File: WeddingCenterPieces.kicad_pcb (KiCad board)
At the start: 2 copper layers, 80 x 57 mm, 58 parts, among them J1 USB_C_Receptacle_USB2.0_16P, J2 DBG, J5 WS2812, K1 SW_Push, K2 SW_Push, K3 SW_Push, K4 SW_Push, SW1 Btn_OnBoard, SW2 RST, SW3 BOOT, U1 RP2040, U2 TPD2E2U06, U4 TXS0101DBV, U5 W25Q128JVSIQ, U6 TVS0500DRV, U7 AP2112K-3.3, Y1 12MHz

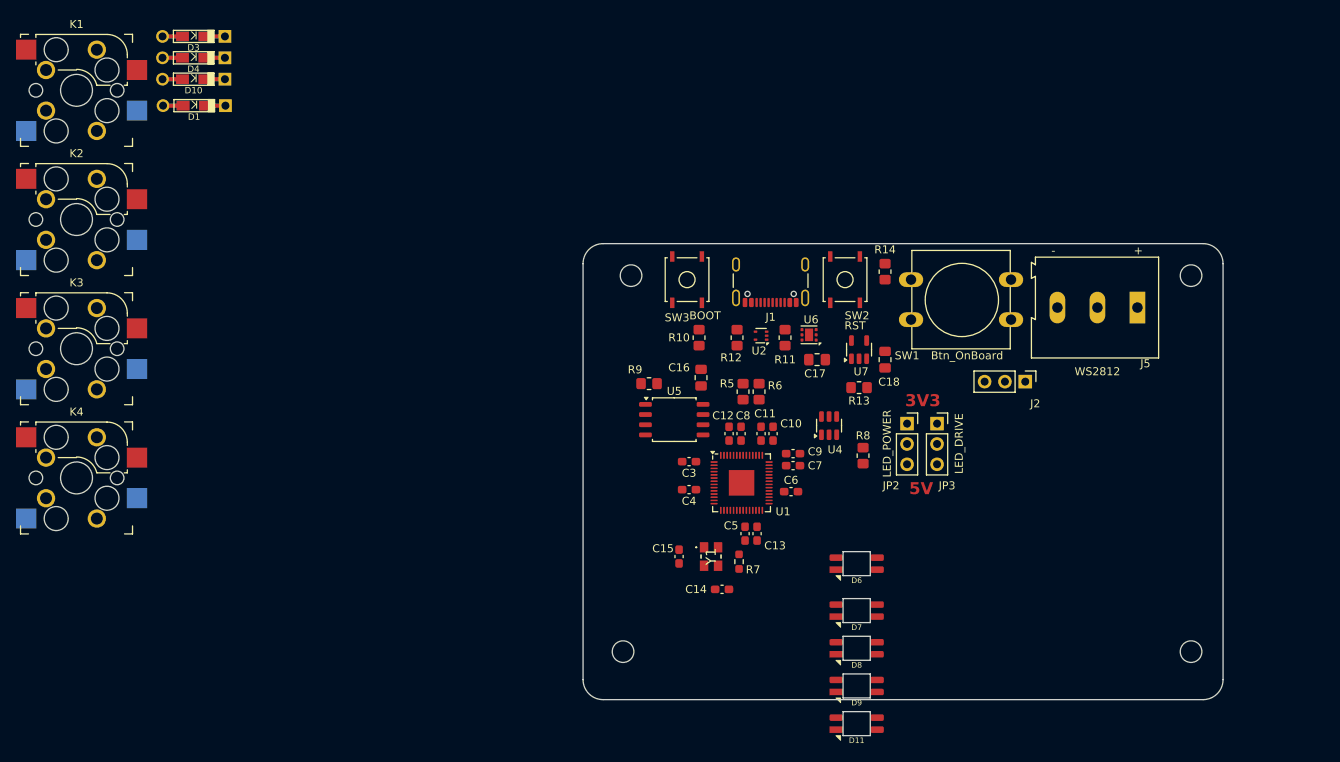
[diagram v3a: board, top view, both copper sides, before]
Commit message: Added testpoints, finished placing components, fixed footprint mapping, and ready to start routing tracks.
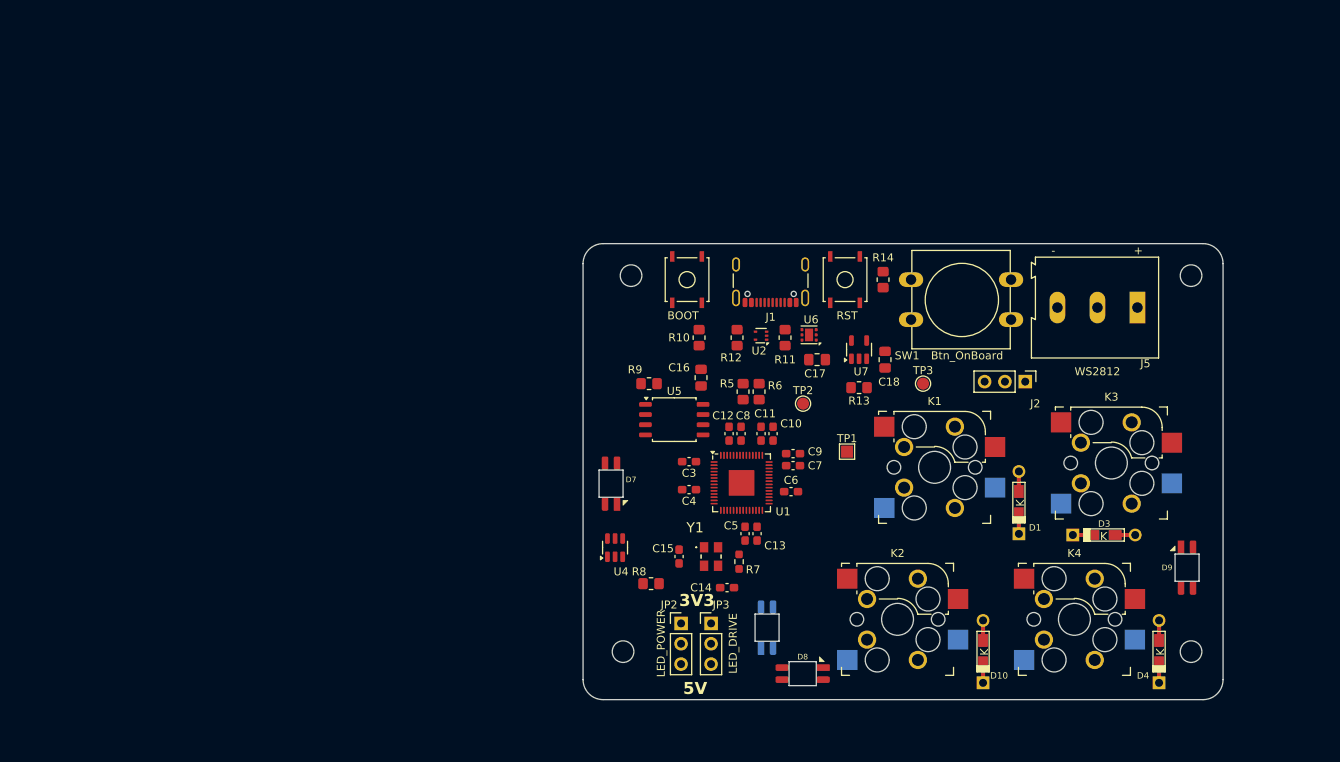
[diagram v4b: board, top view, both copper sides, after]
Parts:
- removed D11: ~, Extra:SK6812-MINI-E_ReverseMount
- added TP1: GND, TestPoint:TestPoint_Pad_1.5x1.5mm, F.Cu at (119.0, 93.0)
- added TP2: VBUS, TestPoint:TestPoint_Pad_D1.5mm, F.Cu at (113.5, 87.0)
- added TP3: 3V3, TestPoint:TestPoint_Pad_D1.5mm, F.Cu at (128.5, 84.5)
- D1, D10, D3, D4: value DIODE -> 1N4148W
- D6: moved to B.Cu
- JP2, JP3: footprint Connector_PinSocket_2.54mm:PinSocket_1x03_P2.54mm_Vertical -> Connector_PinHeader_2.54mm:PinHeader_1x03_P2.54mm_Vertical
- moved D4 141.7 mm to (158.0, 118.0), turned to -90 degrees
- moved K3 130.1 mm to (152.0, 94.4)
- moved D3 129.7 mm to (151.1, 103.4), turned to 180 degrees
- moved K4 126.0 mm to (147.4, 114.0)
- moved D10 121.9 mm to (136.0, 118.0), turned to -90 degrees
- moved K1 117.2 mm to (129.9, 95.0)
- moved D1 114.4 mm to (140.5, 99.4), turned to -90 degrees
- moved K2 114.1 mm to (125.3, 114.0)
- moved D9 43.9 mm to (161.5, 107.5), turned to -90 degrees
- moved JP2 37.7 mm to (98.2, 114.5)
- moved JP3 37.7 mm to (102.0, 114.5)
- moved D7 34.6 mm to (89.5, 97.0), turned to 90 degrees
- moved R8 31.0 mm to (94.5, 109.5), turned to 180 degrees
- moved U4 30.8 mm to (90.0, 105.0)
- moved D6 13.8 mm to (109.0, 115.0), turned to 90 degrees
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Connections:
- D1 pad 1: Net-(D1-K) -> /Key Switches/ROW_1
- D1 pad 2: /Key Switches/ROW_1 -> Net-(D1-A)
- D10 pad 1: Net-(D10-K) -> /Key Switches/ROW_2
- D10 pad 2: /Key Switches/ROW_2 -> Net-(D10-A)
- D3 pad 1: Net-(D3-K) -> /Key Switches/ROW_1
- D3 pad 2: /Key Switches/ROW_1 -> Net-(D3-A)
- D4 pad 1: Net-(D4-K) -> /Key Switches/ROW_2
- D4 pad 2: /Key Switches/ROW_2 -> Net-(D4-A)
- D9 pad 4: Net-(D11-DIN) -> /External Connectors/LED_Data
- K1 pad 2: Net-(D1-K) -> Net-(D1-A)
- K2 pad 2: Net-(D10-K) -> Net-(D10-A)
- K3 pad 2: Net-(D3-K) -> Net-(D3-A)
- K4 pad 2: Net-(D4-K) -> Net-(D4-A)

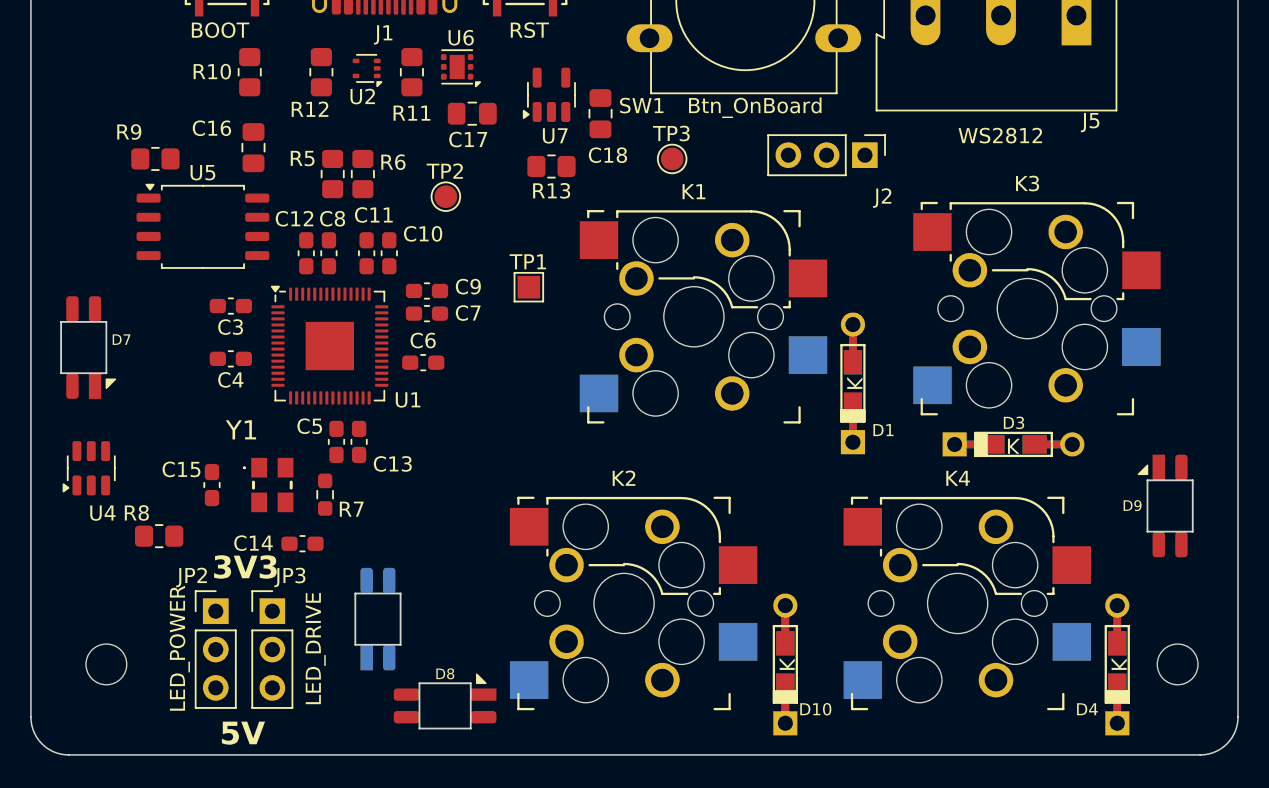
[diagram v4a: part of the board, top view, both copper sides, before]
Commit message: Updating SK6812 circuit to match suggested application from datasheet, adding a resistor at the last DOut and filter caps to each LED.
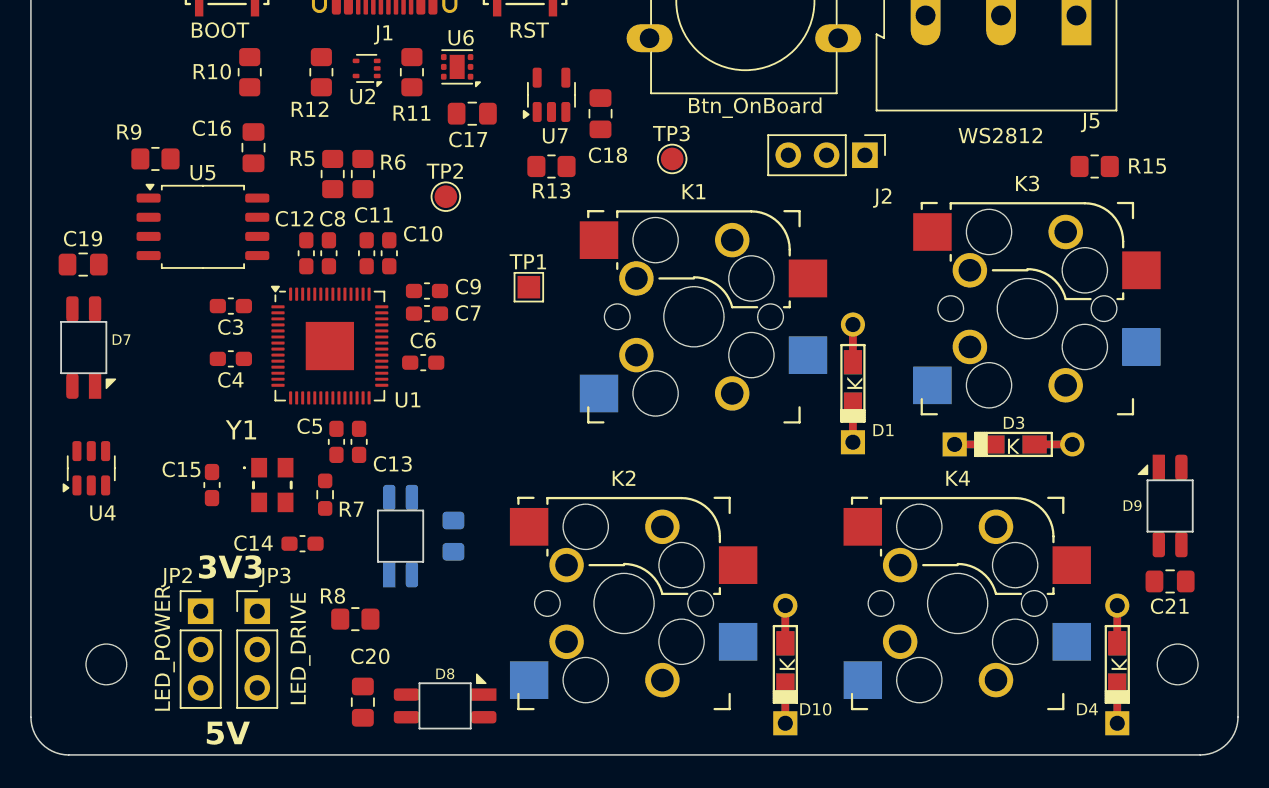
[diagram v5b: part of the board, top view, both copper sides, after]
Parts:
- added C19: 100nF, Capacitor_SMD:C_0805_2012Metric_Pad1.18x1.45mm_HandSolder, F.Cu at (89.5, 91.5)
- added C2: 100nF, Capacitor_SMD:C_0805_2012Metric_Pad1.18x1.45mm_HandSolder, B.Cu at (114.0, 109.5)
- added C20: 100nF, Capacitor_SMD:C_0805_2012Metric_Pad1.18x1.45mm_HandSolder, F.Cu at (108.0, 120.5)
- added C21: 100nF, Capacitor_SMD:C_0805_2012Metric_Pad1.18x1.45mm_HandSolder, F.Cu at (161.5, 112.5)
- added R15: 470, Resistor_SMD:R_0805_2012Metric_Pad1.20x1.40mm_HandSolder, F.Cu at (156.5, 85.0)
- moved R8 14.1 mm to (107.5, 115.0)
- moved D6 5.70 mm to (110.5, 109.5)
- moved JP2 1.00 mm to (97.2, 114.5)
- moved JP3 1.00 mm to (101.0, 114.5)
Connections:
- D9 pad 4: /External Connectors/LED_Data -> Net-(D9-DOUT)
- JP3 pad 2: /Lighting/DIN -> Net-(JP3-C)
- R8 pad 1: Net-(JP3-B) -> /Lighting/DIN
- R8 pad 2: Net-(U4-B) -> Net-(JP3-C)
- U4 pad 4: Net-(U4-B) -> Net-(JP3-B)

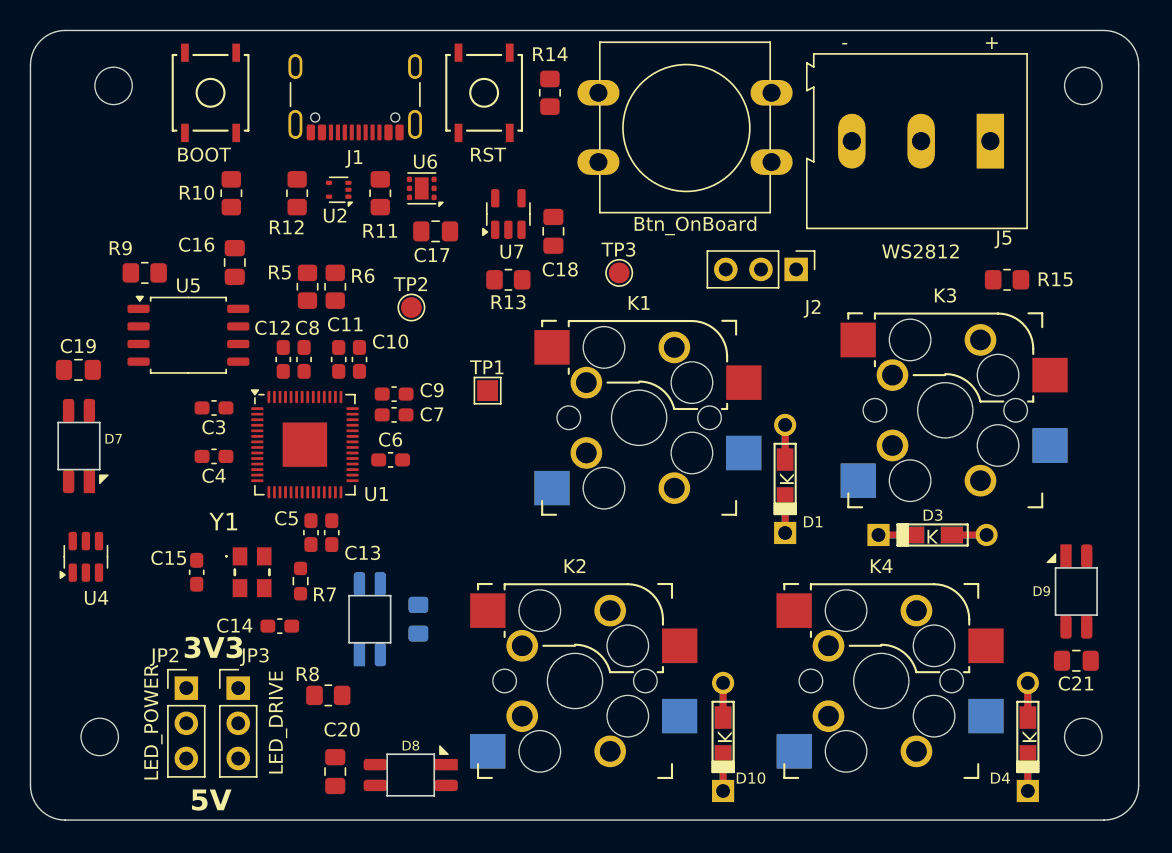
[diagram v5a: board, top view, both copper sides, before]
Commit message: Adding additional LEDs and driver to test per-key LEDs, updating net classes and design constraints, and starting to route tracks.
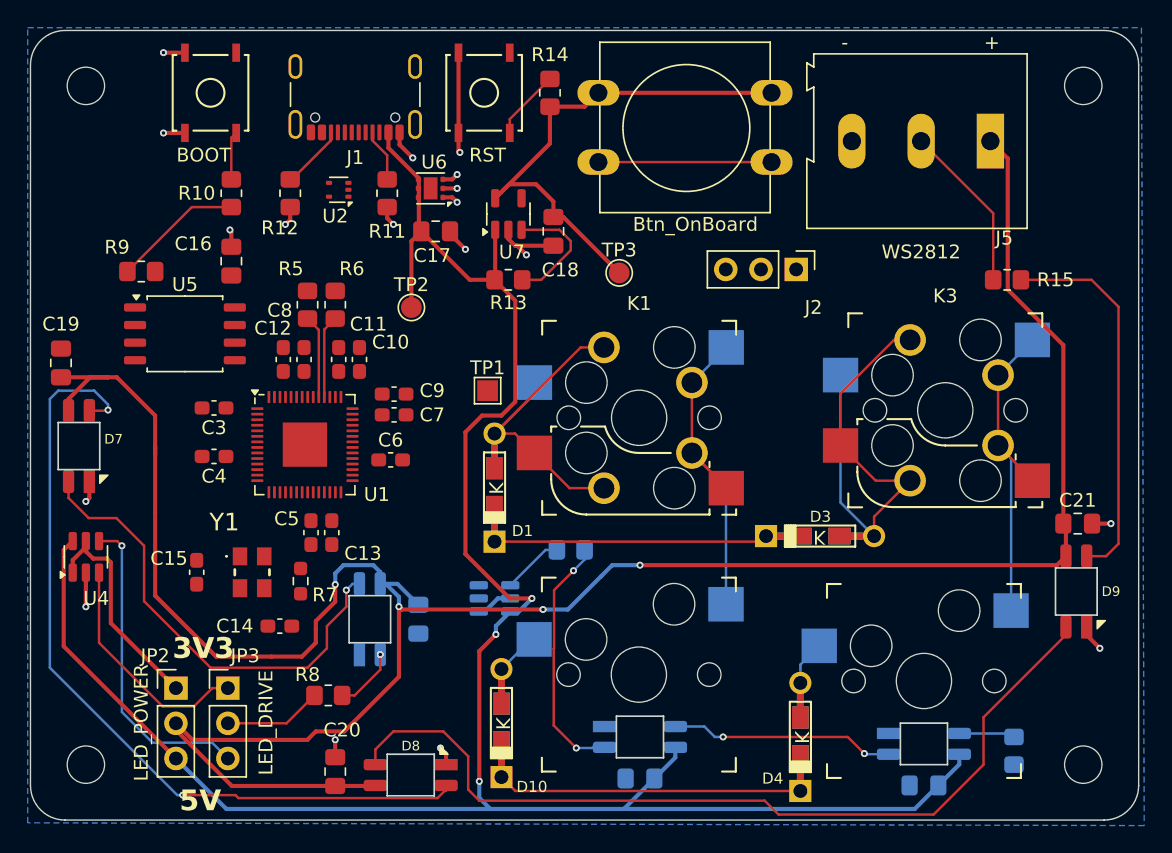
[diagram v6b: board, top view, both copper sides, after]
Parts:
- added C22: 100nF, Capacitor_SMD:C_0805_2012Metric_Pad1.18x1.45mm_HandSolder, B.Cu at (130.0, 121.0)
- added C23: 100nF, Capacitor_SMD:C_0805_2012Metric_Pad1.18x1.45mm_HandSolder, B.Cu at (150.5, 121.5)
- added D11: ~, Extra:SK6812-MINI-E_ReverseMount, B.Cu at (130.0, 118.0)
- added D12: ~, Extra:SK6812-MINI-E_ReverseMount, B.Cu at (150.5, 118.5)
- added R16: 470, Resistor_SMD:R_0805_2012Metric_Pad1.20x1.40mm_HandSolder, B.Cu at (125.0, 104.5)
- added R17: 470, Resistor_SMD:R_0805_2012Metric_Pad1.20x1.40mm_HandSolder, B.Cu at (157.0, 119.0)
- added U8: TXS0101DBV, Package_TO_SOT_SMD:SOT-23-6, B.Cu at (119.5, 108.0)
- K1, K3: moved to B.Cu
- K2, K4: footprint keyswitches:Kailh_socket_MX_optional_reversible -> keyswitches:Kailh_socket_MX
- moved D1 21.0 mm to (119.5, 100.0)
- moved D4 16.4 mm to (141.6, 118.0)
- moved D10 16.0 mm to (120.0, 117.0)
- moved C21 9.90 mm to (161.6, 102.6), turned to 0 degrees
- moved D3 8.12 mm to (143.0, 103.5)
- moved K2 4.63 mm to (129.9, 113.5)
- moved K4 3.08 mm to (150.5, 114.0)
- moved H3 2.24 mm to (90.0, 120.0)
- moved H1 2.00 mm to (90.0, 71.0)
- moved H4 2.00 mm to (162.0, 120.0)
- moved C19 1.36 mm to (88.2, 91.0), turned to 90 degrees
- moved R5 1.30 mm to (106.0, 86.8)
- moved R6 1.30 mm to (108.0, 86.8)
- moved JP2 0.75 mm to (96.5, 114.5)
- moved JP3 0.75 mm to (100.2, 114.5)
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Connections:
- J1 pad S1: GND -> unconnected-(J1-SHIELD-PadS1)_2
- U1 pad 9: unconnected-(U1-GPIO7-Pad9) -> /Lighting/DIN_1
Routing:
- net /Lighting/PowerRail: track 0.00 -> 177.9 mm, vias 0 -> 4
- net VBUS: track 0.00 -> 156.0 mm, vias 0 -> 3
- net Net-(D8-DOUT): track 0.00 -> 63.3 mm
- net Net-(D7-DOUT): track 0.00 -> 59.5 mm, vias 0 -> 2
- net +3V3: track 0.00 -> 56.6 mm
- net GND: track 0.00 -> 37.2 mm, vias 0 -> 18
- net Net-(D3-A): track 0.00 -> 34.1 mm
- net Net-(D6-DOUT): track 0.00 -> 33.8 mm, vias 0 -> 1
- net Net-(D9-DOUT): track 0.00 -> 27.6 mm
- net Net-(D1-A): track 0.00 -> 24.9 mm
- net /Key Switches/COL_2: track 0.00 -> 24.5 mm
- net /Key Switches/COL_1: track 0.00 -> 24.2 mm
- net Net-(JP3-B): track 0.00 -> 22.8 mm, vias 0 -> 1
- net /Key Switches/ROW_2: track 0.00 -> 22.0 mm
- net /Key Switches/ROW_1: track 0.00 -> 19.8 mm
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- added copper zone on B.Cu, net GND
